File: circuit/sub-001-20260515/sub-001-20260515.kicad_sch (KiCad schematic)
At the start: 141 parts, among them J1 Conn_Main, J2 Conn_NeoPixel, J3 Conn_SW_TGL, J4 Conn_Power, Q1 NMOS, Q2 NMOS, Q3 NMOS, Q4 NMOS, Q5 NMOS, Q6 NMOS, Q7 NMOS, Q8 NMOS, U1 LM1117MP-3.3, U10 LM1117MP-3.3, U11 LM1117MP-3.3, U12 LM1117MP-3.3, U13 LM1117MP-3.3, U14 TSSP58038, U15 TSSP58038, U16 TSSP58038, U17 TSSP58038, U18 NE555DR, U19 NE555DR, U20 NE555DR, U21 NE555DR, U22 NE555DR, U23 NE555DR, U24 NE555DR, U25 NE555DR, U9 LM1117MP-3.3

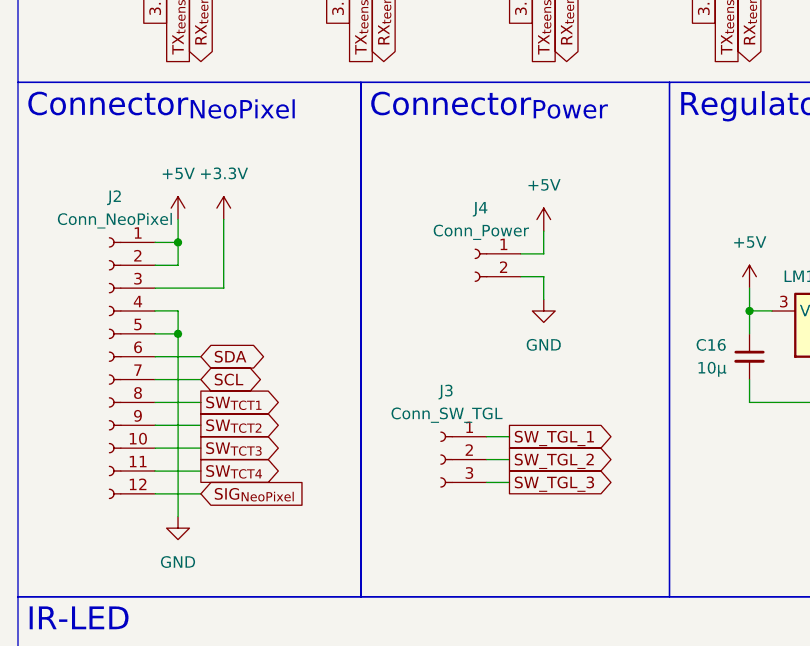
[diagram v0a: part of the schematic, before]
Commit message: Update サブ基板とネオピク基板のラベル名を統一・回路図PDFを作成
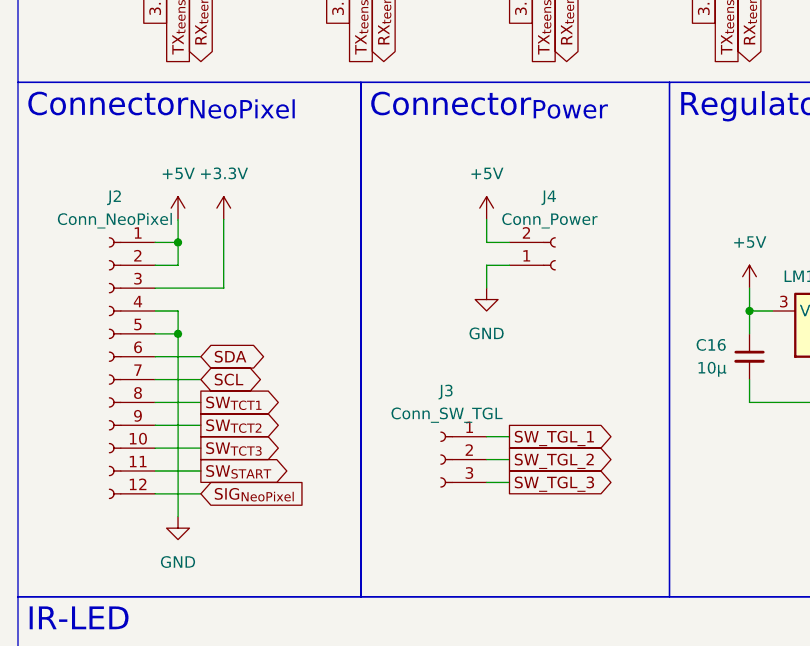
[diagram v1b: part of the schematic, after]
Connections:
- net SW_{TCT4} is gone; now on net SW_{START}: J2.11 (Pin_11)
- net +5V: now also J4.2 (Pin_2); no longer J4.1 (Pin_1)
- net GND: now also J4.1 (Pin_1); no longer J4.2 (Pin_2)
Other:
- moved on the sheet: J4
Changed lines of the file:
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@@
 	(wire
 		(pts
-			(xy 71.12 82.55) (xy 71.12 85.09)
+			(xy 64.77 81.28) (xy 64.77 83.82)
 		)
 		(stroke
@@
 	(wire
 		(pts
-			(xy 71.12 87.63) (xy 71.12 90.17)
+			(xy 64.77 86.36) (xy 64.77 88.9)
 		)
 		(stroke
@@
 	(wire
 		(pts
-			(xy 68.58 85.09) (xy 71.12 85.09)
+			(xy 64.77 83.82) (xy 67.31 83.82)
 		)
 		(stroke
@@
 	(wire
 		(pts
-			(xy 68.58 87.63) (xy 71.12 87.63)
+			(xy 64.77 86.36) (xy 67.31 86.36)
 		)
 		(stroke
@@
 		)
 	)
-	(global_label "SW_{TCT4}"
+	(global_label "SW_{START}"
 		(shape output)
 		(at 33.02 109.22 0)
@@
 		)
 		(property "Intersheetrefs" "${INTERSHEET_REFS}"
-			(at 44.7744 109.22 0)
+			(at 42.2682 109.22 0)
 			(hide yes)
 			(show_name no)
@@
 	(symbol
 		(lib_id "Connector:Conn_01x02_Socket")
-		(at 63.5 85.09 0)
-		(mirror y)
+		(at 72.39 86.36 0)
+		(mirror x)
 		(unit 1)
 		(body_style 1)
@@
 		(fields_autoplaced yes)
 		(property "Reference" "J4"
-			(at 64.135 80.01 0)
+			(at 71.755 78.74 0)
 			(show_name no)
 			(do_not_autoplace no)
@@
 		)
 		(property "Value" "Conn_Power"
-			(at 64.135 82.55 0)
+			(at 71.755 81.28 0)
 			(show_name no)
 			(do_not_autoplace no)
@@
 		)
 		(property "Footprint" "Connector_AMASS:AMASS_XT30U-M_1x02_P5.0mm_Vertical"
-			(at 63.5 85.09 0)
+			(at 72.39 86.36 0)
 			(hide yes)
 			(show_name no)
@@
 		)
 		(property "Datasheet" ""
-			(at 63.5 85.09 0)
+			(at 72.39 86.36 0)
 			(hide yes)
 			(show_name no)
@@
 		)
 		(property "Description" "Generic connector, single row, 01x02, script generated"
-			(at 63.5 85.09 0)
+			(at 72.39 86.36 0)
 			(hide yes)
 			(show_name no)
@@
 	(symbol
 		(lib_id "power:GND")
-		(at 71.12 90.17 0)
+		(at 64.77 88.9 0)
 		(unit 1)
 		(body_style 1)
@@
 		(fields_autoplaced yes)
 		(property "Reference" "#PWR041"
-			(at 71.12 96.52 0)
+			(at 64.77 95.25 0)
 			(hide yes)
 			(show_name no)
@@
 		)
 		(property "Value" "GND"
-			(at 71.12 95.25 0)
+			(at 64.77 93.98 0)
 			(show_name no)
 			(do_not_autoplace no)
@@
 		)
 		(property "Footprint" ""
-			(at 71.12 90.17 0)
+			(at 64.77 88.9 0)
 			(hide yes)
 			(show_name no)
@@
 		)
 		(property "Datasheet" ""
-			(at 71.12 90.17 0)
+			(at 64.77 88.9 0)
 			(hide yes)
 			(show_name no)
@@
 		)
 		(property "Description" "Power symbol creates a global label with name \"GND\" , ground"
-			(at 71.12 90.17 0)
+			(at 64.77 88.9 0)
 			(hide yes)
 			(show_name no)
@@
 	(symbol
 		(lib_id "power:+5V")
-		(at 71.12 82.55 0)
+		(at 64.77 81.28 0)
 		(unit 1)
 		(body_style 1)
@@
 		(fields_autoplaced yes)
 		(property "Reference" "#PWR040"
-			(at 71.12 86.36 0)
+			(at 64.77 85.09 0)
 			(hide yes)
 			(show_name no)
@@
 		)
 		(property "Value" "+5V"
-			(at 71.12 77.47 0)
+			(at 64.77 76.2 0)
 			(show_name no)
 			(do_not_autoplace no)
@@
 		)
 		(property "Footprint" ""
-			(at 71.12 82.55 0)
+			(at 64.77 81.28 0)
 			(hide yes)
 			(show_name no)
@@
 		)
 		(property "Datasheet" ""
-			(at 71.12 82.55 0)
+			(at 64.77 81.28 0)
 			(hide yes)
 			(show_name no)
@@
 		)
 		(property "Description" "Power symbol creates a global label with name \"+5V\""
-			(at 71.12 82.55 0)
+			(at 64.77 81.28 0)
 			(hide yes)
 			(show_name no)

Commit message: Update サブ基板のシンボルとフットプリントの紐づけをした
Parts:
- added U26, U27, U28, U29: HC-SR04, Connector_PinHeader_2.54mm:PinHeader_1x04_P2.54mm_Vertical, symbol @Thrive_symbol_sub:HC-SR04
- C10: renamed from C20; value 10u -> 10μ; footprint (none) -> Capacitor_SMD:C_0805_2012Metric
- C11: renamed from C24; value 10u -> 10μ; footprint (none) -> Capacitor_SMD:C_0805_2012Metric
- C14: renamed from C25; footprint (none) -> Capacitor_SMD:C_0805_2012Metric
- C15: renamed from C26; footprint (none) -> Capacitor_SMD:C_0805_2012Metric
- C17: renamed from C27; footprint (none) -> Capacitor_SMD:C_0805_2012Metric
- C18: renamed from C28; footprint (none) -> Capacitor_SMD:C_0805_2012Metric
- C2: renamed from C18; footprint (none) -> Capacitor_SMD:C_0805_2012Metric
- C21: renamed from C29; footprint (none) -> Capacitor_SMD:C_0805_2012Metric
- C22: renamed from C30; footprint (none) -> Capacitor_SMD:C_0805_2012Metric
- C24: renamed from C31; value 10u -> 10μ; footprint (none) -> Capacitor_SMD:C_0805_2012Metric
- C25: renamed from C32; footprint (none) -> Capacitor_SMD:C_0805_2012Metric
- C27: renamed from C33; footprint (none) -> Capacitor_SMD:C_0805_2012Metric
- C28: renamed from C34; footprint (none) -> Capacitor_SMD:C_0805_2012Metric
- C29: renamed from C35; footprint (none) -> Capacitor_SMD:C_0805_2012Metric
- C3: renamed from C21; footprint (none) -> Capacitor_SMD:C_0805_2012Metric
- C30: renamed from C36; footprint (none) -> Capacitor_SMD:C_0805_2012Metric
- C33: renamed from C37; footprint (none) -> Capacitor_SMD:C_0805_2012Metric
- C34: renamed from C38; footprint (none) -> Capacitor_SMD:C_0805_2012Metric
- C35: renamed from C39; value 10u -> 10μ; footprint (none) -> Capacitor_SMD:C_0805_2012Metric
- C36: renamed from C40; value 10u -> 10μ; footprint (none) -> Capacitor_SMD:C_0805_2012Metric
- C37: renamed from C41; footprint (none) -> Capacitor_SMD:C_0805_2012Metric
- C38: renamed from C42; footprint (none) -> Capacitor_SMD:C_0805_2012Metric
- C39: renamed from C43; footprint (none) -> Capacitor_SMD:C_0805_2012Metric
- C4: renamed from C1; footprint (none) -> Capacitor_SMD:C_0805_2012Metric
- C40: renamed from C44; footprint (none) -> Capacitor_SMD:C_0805_2012Metric
- C43: renamed from C45; footprint (none) -> Capacitor_SMD:C_0805_2012Metric
- C44: renamed from C46; footprint (none) -> Capacitor_SMD:C_0805_2012Metric
- C45: renamed from C47; value 10u -> 10μ; footprint (none) -> Capacitor_SMD:C_0805_2012Metric
- C46: renamed from C48; value 10u -> 10μ; footprint (none) -> Capacitor_SMD:C_0805_2012Metric
- C5: renamed from C22; footprint (none) -> Capacitor_SMD:C_0805_2012Metric
- C8: renamed from C19; footprint (none) -> Capacitor_SMD:C_0805_2012Metric
- C9: renamed from C23; footprint (none) -> Capacitor_SMD:C_0805_2012Metric
- D1: renamed from D3; footprint (none) -> LED_THT:LED_D3.0mm
- D10, D5, D6, D7, D8, D9: footprint (none) -> LED_THT:LED_D3.0mm
- D2: renamed from D4; footprint (none) -> LED_THT:LED_D3.0mm
- J1: renamed from J2; footprint (none) -> Connector_FFC-FPC:JUSHUO_AFA07-S12FCA-00_1x12-1MP_P1.0mm_Horizontal
- J2: renamed from J3; footprint (none) -> Connector_PinSocket_2.54mm:PinSocket_1x03_P2.54mm_Vertical
- J4: renamed from J1; footprint (none) -> @Thrive_footprint_main:AFC01-S18FCA-00
- Q1, Q2, Q3, Q4, Q5, Q6, Q7, Q8: value NMOS -> BSS138; footprint (none) -> Package_TO_SOT_SMD:SOT-23
- R1: footprint (none) -> Resistor_SMD:R_0805_2012Metric
- R10: renamed from R16; footprint (none) -> Resistor_SMD:R_0805_2012Metric
- R11: renamed from R17; footprint (none) -> Resistor_SMD:R_0805_2012Metric
- R12: renamed from R18; footprint (none) -> Resistor_SMD:R_0805_2012Metric
- R13: renamed from R19; footprint (none) -> Resistor_SMD:R_0805_2012Metric
- R14: renamed from R20; footprint (none) -> Resistor_SMD:R_0805_2012Metric
- R17: renamed from R21; footprint (none) -> Resistor_SMD:R_0805_2012Metric
- R18: renamed from R22; footprint (none) -> Resistor_SMD:R_0805_2012Metric
- R19: renamed from R23; footprint (none) -> Resistor_SMD:R_0805_2012Metric
- R2: renamed from R12; footprint (none) -> Resistor_SMD:R_0805_2012Metric
- R20: renamed from R24; footprint (none) -> Resistor_SMD:R_0805_2012Metric
- R21: renamed from R25; footprint (none) -> Resistor_SMD:R_0805_2012Metric
- R22: renamed from R26; footprint (none) -> Resistor_SMD:R_0805_2012Metric
- R23: renamed from R27; footprint (none) -> Resistor_SMD:R_0805_2012Metric
- R24: renamed from R28; footprint (none) -> Resistor_SMD:R_0805_2012Metric
- R25: renamed from R29; footprint (none) -> Resistor_SMD:R_0805_2012Metric
- R26: renamed from R30; footprint (none) -> Resistor_SMD:R_0805_2012Metric
- R27: renamed from R31; footprint (none) -> Resistor_SMD:R_0805_2012Metric
- R28: renamed from R32; footprint (none) -> Resistor_SMD:R_0805_2012Metric
- R29: renamed from R33; footprint (none) -> Resistor_SMD:R_0805_2012Metric
- R3: renamed from R2; footprint (none) -> Resistor_SMD:R_0805_2012Metric
- R30: renamed from R34; footprint (none) -> Resistor_SMD:R_0805_2012Metric
- R31: renamed from R35; footprint (none) -> Resistor_SMD:R_0805_2012Metric
- R32: renamed from R36; footprint (none) -> Resistor_SMD:R_0805_2012Metric
- R33: renamed from R37; footprint (none) -> Resistor_SMD:R_0805_2012Metric
- R34: renamed from R38; footprint (none) -> Resistor_SMD:R_0805_2012Metric
- R37: renamed from R39; footprint (none) -> Resistor_SMD:R_0805_2012Metric
- R38: renamed from R40; footprint (none) -> Resistor_SMD:R_0805_2012Metric
- R39: renamed from R41; footprint (none) -> Resistor_SMD:R_0805_2012Metric
- R4: renamed from R13; footprint (none) -> Resistor_SMD:R_0805_2012Metric
- R40: renamed from R42; footprint (none) -> Resistor_SMD:R_0805_2012Metric
- R41: renamed from R43; footprint (none) -> Resistor_SMD:R_0805_2012Metric
- R42: renamed from R44; footprint (none) -> Resistor_SMD:R_0805_2012Metric
- R43: renamed from R45; footprint (none) -> Resistor_SMD:R_0805_2012Metric
- R44: renamed from R46; footprint (none) -> Resistor_SMD:R_0805_2012Metric
- R5: renamed from R9; footprint (none) -> Resistor_SMD:R_0805_2012Metric
- R6: renamed from R14; footprint (none) -> Resistor_SMD:R_0805_2012Metric
- R7: renamed from R10; footprint (none) -> Resistor_SMD:R_0805_2012Metric
- R8: renamed from R15; footprint (none) -> Resistor_SMD:R_0805_2012Metric
- R9: renamed from R11; footprint (none) -> Resistor_SMD:R_0805_2012Metric
- renumbered C2 to C1, C8 to C12, C16 to C13, C4 to C16, C17 to C19, C9 to C20, C5 to C23, C10 to C26, C6 to C31, C11 to C32, C12 to C41, C13 to C42, C14 to C47, C15 to C48, C7 to C6, C3 to C7, D1 to D3, D2 to D4, J4 to J3, R3 to R15, R4 to R16, R5 to R35, R6 to R36, R7 to R45, R8 to R46, U2 to U1, U8 to U10, U20 to U12, U21 to U13, U12 to U14, U13 to U15, U4 to U16, U5 to U17, U22 to U18, U23 to U19, U9 to U2, U14 to U20, U15 to U21, U24 to U22, U25 to U23, U16 to U24, U17 to U25, U18 to U4, U19 to U5, U10 to U7, U7 to U8, U1 to U9
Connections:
- net RX_{ESP32C301}-TX_{teensy} is gone; now on net TX_{teensy}-RX_{ESP32C301}: U16.8 (RX_D7)
- net RX_{ESP32C302}-TX_{teensy} is gone; now on net TX_{teensy}-RX_{ESP32C302}: U17.8 (RX_D7)
- net SW_TCT_1 is gone; now on net SW_{TCT1}: U16.9 (SCK_D8)
- net SW_TCT_2 is gone; now on net SW_{TCT2}: U16.10 (MISO_D9)
- net SW_TCT_3 is gone; now on net SW_{TCT3}: U16.11 (MOSI_D10)
- net TX_{ESP32C301}-RX_{teensy} is gone; now on net RX_{teensy}-TX_{ESP32C301}: U16.7 (TX_D6)
- net TX_{ESP32C302}-RX_{teensy} is gone; now on net RX_{teensy}-TX_{ESP32C302}: U17.7 (TX_D6)
- net +3.3V: now also U26.4 (VCC), U27.4 (VCC), U28.4 (VCC), U29.4 (VCC)
- net GND: now also U26.1 (GND), U27.1 (GND), U28.1 (GND), U29.1 (GND)
- net SW_TGL_1 renamed SW_{TGL1}
- net SW_TGL_2 renamed SW_{TGL2}
- net SW_TGL_3 renamed SW_{TGL3}
- net USS_1 renamed USS1
- net USS1: now also U26.2 (Echo)
- net USS_2 renamed USS2
- net USS2: now also U27.2 (Echo)
- net USS_3 renamed USS3
- net USS3: now also U28.2 (Echo)
- net USS_4 renamed USS4
- net USS4: now also U29.2 (Echo)
- net USS_EN renamed USS_{EN}
- net USS_{EN}: now also U26.3 (Trig), U27.3 (Trig), U28.3 (Trig), U29.3 (Trig)
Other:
- moved on the sheet: U16, U17

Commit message: Update サブ基板の回路図・回路図PDF・READMEを更新
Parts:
- U11, U14, U15, U2, U7: value LM1117MP-3.3 -> LM1117GS-3.3
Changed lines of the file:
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@@
 		)
 	)
-	(text_box "Regulator_{3.3V}"
+	(text_box "3-terminal regulator | 3.3V"
 		(exclude_from_sim no)
 		(at 85.09 66.04 0)
@@
 		)
 	)
-	(text_box "Linear-Regulator"
+	(text_box "3-terminal regulator | 3.3V | UnitV"
 		(exclude_from_sim no)
 		(at 12.7 241.3 0)
@@
 		(effects
 			(font
-				(face "游ゴシック")
+				(face "ヒラギノ丸ゴ Pro W4")
 				(size 1.27 1.27)
 				(bold yes)
@@
 			)
 		)
-		(property "Value" "LM1117MP-3.3"
+		(property "Value" "LM1117GS-3.3"
 			(at 35.56 256.54 0)
 			(show_name no)
@@
 			)
 		)
-		(property "Value" "LM1117MP-3.3"
+		(property "Value" "LM1117GS-3.3"
 			(at 157.48 256.54 0)
 			(show_name no)
@@
 			)
 		)
-		(property "Value" "LM1117MP-3.3"
+		(property "Value" "LM1117GS-3.3"
 			(at 198.12 256.54 0)
 			(show_name no)
@@
 			)
 		)
-		(property "Value" "LM1117MP-3.3"
+		(property "Value" "LM1117GS-3.3"
 			(at 76.2 256.54 0)
 			(show_name no)
@@
 			)
 		)
-		(property "Value" "LM1117MP-3.3"
+		(property "Value" "LM1117GS-3.3"
 			(at 116.84 256.54 0)
 			(show_name no)

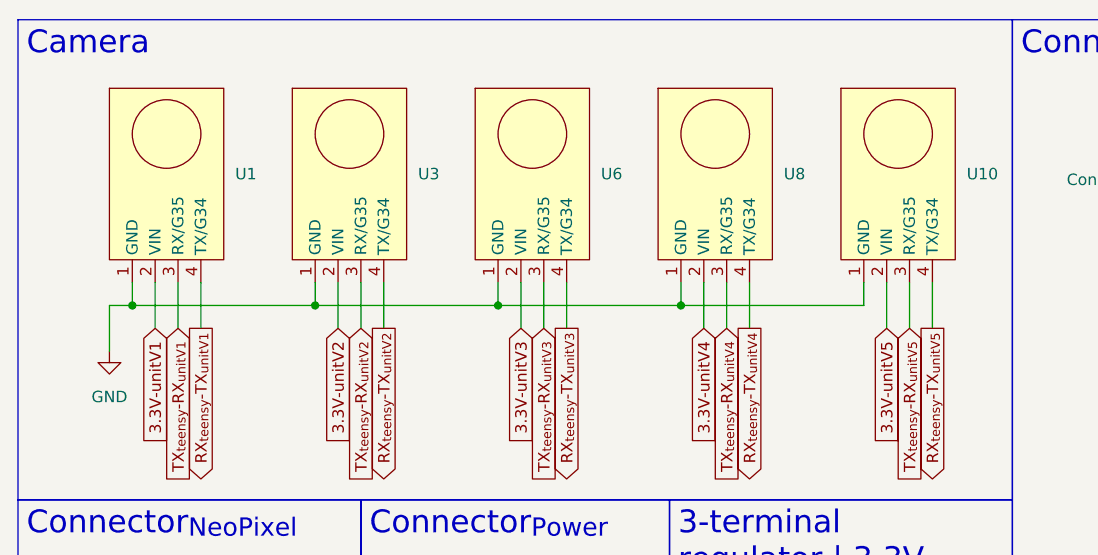
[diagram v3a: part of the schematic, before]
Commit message: Update サブ基板のフットプリント割り当てを進めた
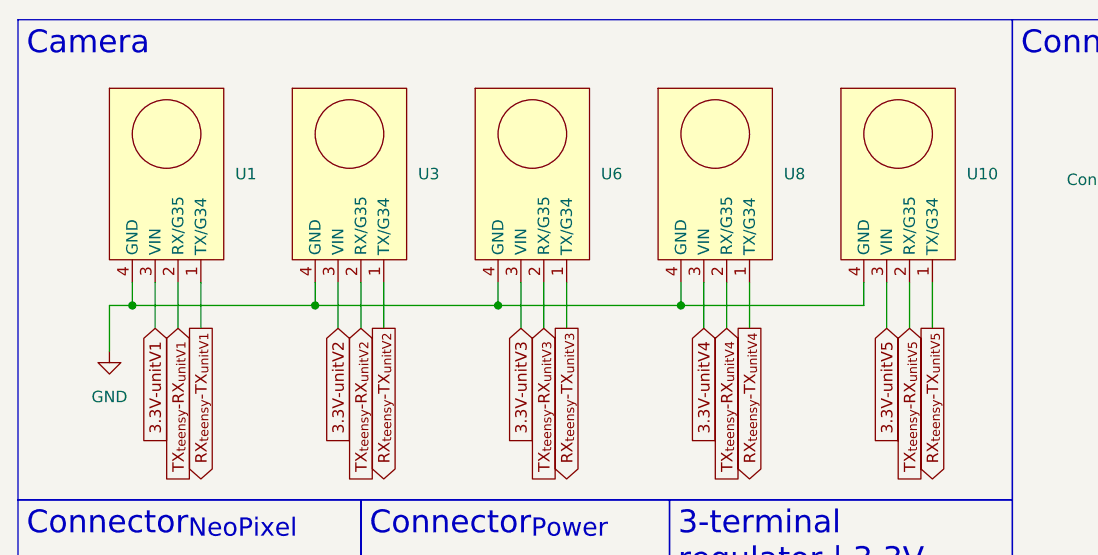
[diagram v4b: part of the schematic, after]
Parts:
- J1: footprint Connector_FFC-FPC:JUSHUO_AFA07-S12FCA-00_1x12-1MP_P1.0mm_Horizontal -> @Thrive_footprint_sub:AFC01-S12FCA-00
- U1, U10, U3, U6, U8: footprint (none) -> Connector:NS-Tech_Grove_1x04_P2mm_Vertical
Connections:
- net 3.3V-unitV1: now also U1.3 (VIN); no longer U1.2 (VIN)
- net 3.3V-unitV2: now also U3.3 (VIN); no longer U3.2 (VIN)
- net 3.3V-unitV3: now also U6.3 (VIN); no longer U6.2 (VIN)
- net 3.3V-unitV4: now also U8.3 (VIN); no longer U8.2 (VIN)
- net 3.3V-unitV5: now also U10.3 (VIN); no longer U10.2 (VIN)
- net GND: now also U1.4 (GND), U10.4 (GND), U3.4 (GND), U6.4 (GND), U8.4 (GND); no longer U1.1 (GND), U10.1 (GND), U3.1 (GND), U6.1 (GND), U8.1 (GND)
- net RX_{teensy}-TX_{unitV1}: now also U1.1 (TX/G34); no longer U1.4 (TX/G34)
- net RX_{teensy}-TX_{unitV2}: now also U3.1 (TX/G34); no longer U3.4 (TX/G34)
- net RX_{teensy}-TX_{unitV3}: now also U6.1 (TX/G34); no longer U6.4 (TX/G34)
- net RX_{teensy}-TX_{unitV4}: now also U8.1 (TX/G34); no longer U8.4 (TX/G34)
- net RX_{teensy}-TX_{unitV5}: now also U10.1 (TX/G34); no longer U10.4 (TX/G34)
- net TX_{teensy}-RX_{unitV1}: now also U1.2 (RX/G35); no longer U1.3 (RX/G35)
- net TX_{teensy}-RX_{unitV2}: now also U3.2 (RX/G35); no longer U3.3 (RX/G35)
- net TX_{teensy}-RX_{unitV3}: now also U6.2 (RX/G35); no longer U6.3 (RX/G35)
- net TX_{teensy}-RX_{unitV4}: now also U8.2 (RX/G35); no longer U8.3 (RX/G35)
- net TX_{teensy}-RX_{unitV5}: now also U10.2 (RX/G35); no longer U10.3 (RX/G35)
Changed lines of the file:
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@@
 			)
 		)
-		(property "Footprint" ""
+		(property "Footprint" "Connector:NS-Tech_Grove_1x04_P2mm_Vertical"
 			(at 29.21 25.4 0)
 			(hide yes)
@@
 			)
 		)
-		(property "Footprint" ""
+		(property "Footprint" "Connector:NS-Tech_Grove_1x04_P2mm_Vertical"
 			(at 90.17 25.4 0)
 			(hide yes)
@@
 			)
 		)
-		(property "Footprint" ""
+		(property "Footprint" "Connector:NS-Tech_Grove_1x04_P2mm_Vertical"
 			(at 110.49 25.4 0)
 			(hide yes)
@@
 			)
 		)
-		(property "Footprint" "Connector_FFC-FPC:JUSHUO_AFA07-S12FCA-00_1x12-1MP_P1.0mm_Horizontal"
+		(property "Footprint" "@Thrive_footprint_sub:AFC01-S12FCA-00"
 			(at 22.86 96.52 0)
 			(hide yes)
@@
 			)
 		)
-		(property "Footprint" ""
+		(property "Footprint" "Connector:NS-Tech_Grove_1x04_P2mm_Vertical"
 			(at 49.53 25.4 0)
 			(hide yes)
@@
 			)
 		)
-		(property "Footprint" ""
+		(property "Footprint" "Connector:NS-Tech_Grove_1x04_P2mm_Vertical"
 			(at 69.85 25.4 0)
 			(hide yes)

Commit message: Update サブ基板のフットプリント割り当てを進めた
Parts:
- J4: footprint @Thrive_footprint_main:AFC01-S18FCA-00 -> @Thrive_footprint_sub:AFC01-S18FCA-00
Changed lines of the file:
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@@
 			)
 		)
-		(property "Footprint" "@Thrive_footprint_main:AFC01-S18FCA-00"
+		(property "Footprint" "@Thrive_footprint_sub:AFC01-S18FCA-00"
 			(at 133.35 53.34 0)
 			(hide yes)

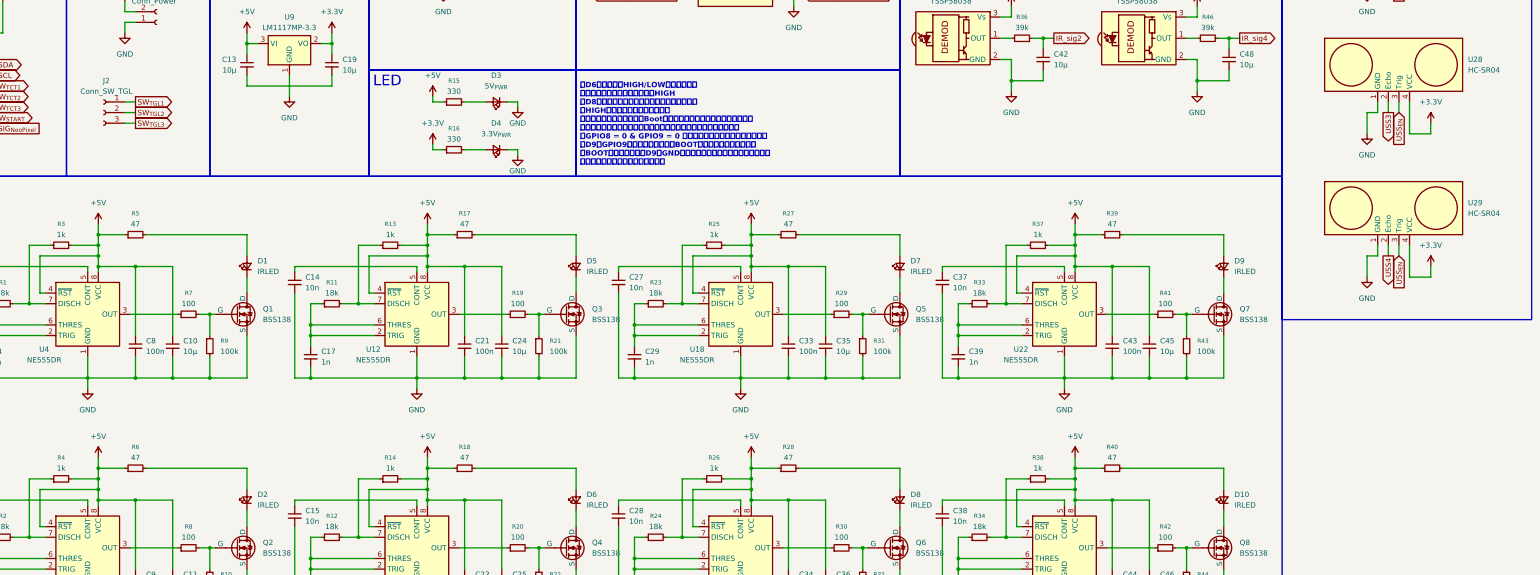
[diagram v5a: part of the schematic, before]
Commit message: Update サブ基板にトグルSWのプルアップ抵抗を追加
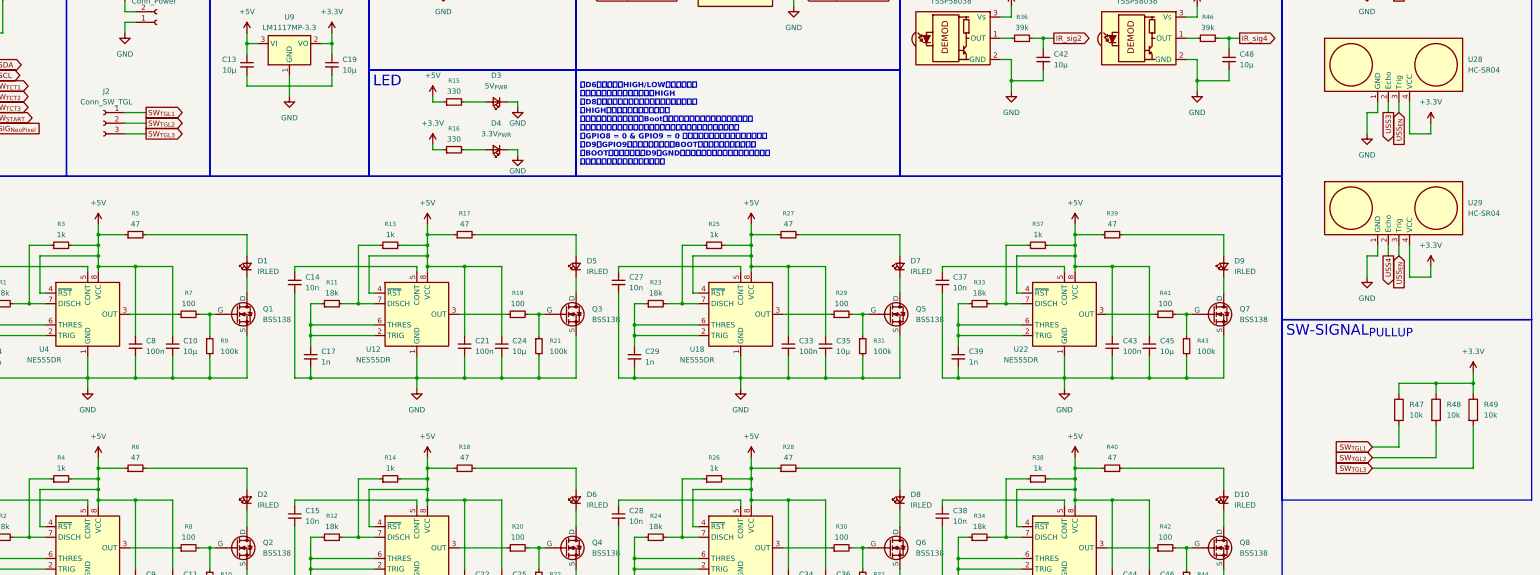
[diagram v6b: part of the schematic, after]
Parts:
- added R47, R48, R49: 10k, symbol Device:R
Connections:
- net +3.3V: now also R47.1, R48.1, R49.1
- net SW_{TGL1}: now also R47.2
- net SW_{TGL2}: now also R48.2
- net SW_{TGL3}: now also R49.2
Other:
- moved on the sheet: J2
